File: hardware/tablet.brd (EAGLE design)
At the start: 198 x 124 mm, 16 parts, among them IC2 MCP3201, IC4 MAX6104EUR, IC5 MAX4514EUK

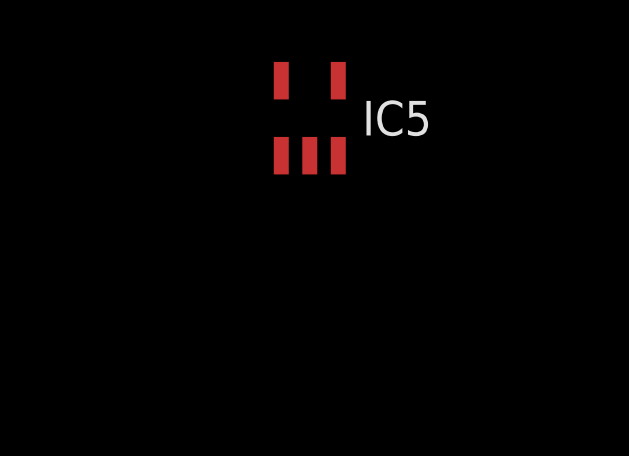
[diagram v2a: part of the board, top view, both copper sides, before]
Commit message: Add protection diodes to common signal
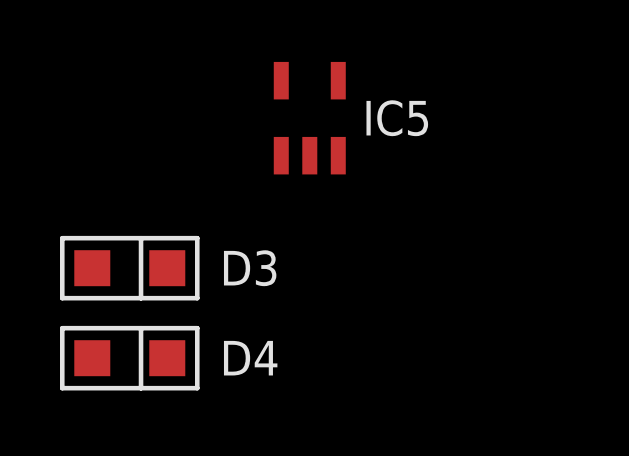
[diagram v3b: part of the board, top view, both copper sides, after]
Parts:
- added D3, D4: 5V1, 0jpe:SOD323
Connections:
- new net N$5: D3.2, D4.2
- net GND: now also D3.1
- net SIG: now also D4.1
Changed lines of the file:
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@@
 <element name="C7" library="0jpe" package="0603" value="100nF" x="-134" y="-122"/>
 <element name="IC5" library="0jpe" package="SOT23_5" value="MAX4514EUK" x="-133" y="-127"/>
+<element name="D3" library="0jpe" package="SOD323" value="5V1" x="-139" y="-132"/>
+<element name="D4" library="0jpe" package="SOD323" value="5V1" x="-139" y="-135"/>
 </elements>
 <signals>
@@
 <signal name="SIG">
 <contactref element="R2" pad="1"/>
+<contactref element="D4" pad="1"/>
+<wire x1="-140.25" y1="-135" x2="-99.75" y2="-88" width="0" layer="19" extent="1-1"/>
 </signal>
 <signal name="GND">
@@
 <contactref element="C7" pad="2"/>
 <contactref element="IC5" pad="3"/>
+<contactref element="D3" pad="1"/>
 <wire x1="-133.25" y1="-116" x2="-133.25" y2="-119" width="0" layer="19" extent="1-1"/>
 <wire x1="-133.25" y1="-122" x2="-133.25" y2="-119" width="0" layer="19" extent="1-1"/>
@@
 <wire x1="-122.365" y1="-94.6" x2="-128.25" y2="-100" width="0" layer="19" extent="1-1"/>
 <wire x1="-121.095" y1="-94.6" x2="-122.365" y2="-94.6" width="0" layer="19" extent="1-1"/>
+<wire x1="-140.25" y1="-132" x2="-132.05" y2="-128.25" width="0" layer="19" extent="1-1"/>
 <wire x1="-113.635" y1="-85.6" x2="-121.095" y2="-94.6" width="0" layer="19" extent="1-1"/>
 <wire x1="-111.095" y1="-80.4" x2="-113.635" y2="-85.6" width="0" layer="19" extent="1-1"/>
@@
 <contactref element="IC5" pad="4"/>
 </signal>
+<signal name="N$5">
+<contactref element="D4" pad="2"/>
+<contactref element="D3" pad="2"/>
+<wire x1="-137.75" y1="-132" x2="-137.75" y2="-135" width="0" layer="19" extent="1-1"/>
+</signal>
 </signals>

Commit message: Fix precision rectifier op amp orientation
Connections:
- net GND: now also IC1.3; no longer IC1.2
- net N$2: now also IC1.2; no longer IC1.3
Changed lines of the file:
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@@
 <setting verticaltext="up"/>
 </settings>
-<grid distance="1" unitdist="mm" unit="mm" style="lines" multiple="1" display="yes" altdistance="0.1" altunitdist="mm" altunit="mm"/>
+<grid distance="1" unitdist="mm" unit="mm" style="lines" multiple="1" display="yes" altdistance="0.0375" altunitdist="mm" altunit="mm"/>
 <layers>
 <layer number="1" name="Top" color="4" fill="1" visible="yes" active="yes"/>
@@
 <wire x1="-90" y1="62" x2="-90" y2="-62" width="0.15" layer="21"/>
 <dimension x1="76" y1="48" x2="76" y2="-48" x3="81" y3="0" textsize="2" layer="47"/>
-<dimension x1="76" y1="-48" x2="-76" y2="-48" x3="0" y3="-53" textsize="2" layer="47"/>
+<dimension x1="76" y1="-48" x2="-76" y2="-47.55" x3="-0.014803125" y3="-52.774978125" textsize="2" layer="47"/>
 <dimension x1="-106" y1="-62" x2="90" y2="-62" x3="-8" y3="-67" textsize="2" layer="47"/>
 <dimension x1="90" y1="-62" x2="90" y2="62" x3="95" y3="0" textsize="2" layer="47"/>
@@
 <contactref element="R2" pad="2"/>
 <contactref element="R1" pad="1"/>
-<contactref element="IC1" pad="3"/>
-<wire x1="-99.75" y1="-85" x2="-112.365" y2="-85.6" width="0" layer="19" extent="1-1"/>
+<contactref element="IC1" pad="2"/>
+<wire x1="-99.75" y1="-85" x2="-113.635" y2="-85.6" width="0" layer="19" extent="1-1"/>
 <wire x1="-98.25" y1="-88" x2="-99.75" y2="-85" width="0" layer="19" extent="1-1"/>
 <wire x1="-98.05" y1="-81.25" x2="-99.75" y2="-85" width="0" layer="19" extent="1-1"/>
-</signal>
-<signal name="N$3">
-<contactref element="D1" pad="3"/>
-<contactref element="IC1" pad="1"/>
-<wire x1="-99" y1="-78.75" x2="-114.905" y2="-85.6" width="0" layer="19" extent="1-1"/>
 </signal>
 <signal name="SIG">
@@
 </signal>
 <signal name="GND">
-<contactref element="IC1" pad="2"/>
 <contactref element="IC1" pad="5"/>
 <contactref element="IC2" pad="3"/>
@@
 <contactref element="IC5" pad="3"/>
 <contactref element="D3" pad="1"/>
+<contactref element="IC1" pad="3"/>
 <wire x1="-133.25" y1="-116" x2="-133.25" y2="-119" width="0" layer="19" extent="1-1"/>
 <wire x1="-133.25" y1="-122" x2="-133.25" y2="-119" width="0" layer="19" extent="1-1"/>
@@
 <wire x1="-121.095" y1="-94.6" x2="-122.365" y2="-94.6" width="0" layer="19" extent="1-1"/>
 <wire x1="-140.25" y1="-132" x2="-132.05" y2="-128.25" width="0" layer="19" extent="1-1"/>
-<wire x1="-113.635" y1="-85.6" x2="-121.095" y2="-94.6" width="0" layer="19" extent="1-1"/>
-<wire x1="-111.095" y1="-80.4" x2="-113.635" y2="-85.6" width="0" layer="19" extent="1-1"/>
+<wire x1="-112.365" y1="-85.6" x2="-121.095" y2="-94.6" width="0" layer="19" extent="1-1"/>
+<wire x1="-111.095" y1="-80.4" x2="-112.365" y2="-85.6" width="0" layer="19" extent="1-1"/>
 </signal>
 <signal name="+5V">
-<contactref element="IC1" pad="8"/>
 <contactref element="C2" pad="1"/>
 <contactref element="C4" pad="1"/>
@@
 <contactref element="C7" pad="1"/>
 <contactref element="IC5" pad="5"/>
+<contactref element="IC1" pad="8"/>
 <wire x1="-134.75" y1="-122" x2="-134.75" y2="-116" width="0" layer="19" extent="1-1"/>
 <wire x1="-133.95" y1="-125.75" x2="-134.75" y2="-122" width="0" layer="19" extent="1-1"/>
@@
 </signal>
 <signal name="-5V">
+<contactref element="C3" pad="2"/>
 <contactref element="IC1" pad="4"/>
-<contactref element="C3" pad="2"/>
 <wire x1="-111.095" y1="-85.6" x2="-128.25" y2="-103" width="0" layer="19" extent="1-1"/>
 </signal>
@@
 <wire x1="-137.75" y1="-132" x2="-137.75" y2="-135" width="0" layer="19" extent="1-1"/>
 </signal>
+<signal name="N$7">
+</signal>
+<signal name="N$8">
+</signal>
+<signal name="N$9">
+</signal>
+<signal name="N$10">
+</signal>
+<signal name="N$11">
+</signal>
+<signal name="N$12">
+</signal>
+<signal name="N$14">
+</signal>
+<signal name="N$15">
+</signal>
+<signal name="N$16">
+</signal>
+<signal name="N$17">
+</signal>
+<signal name="N$18">
+</signal>
+<signal name="N$19">
+</signal>
+<signal name="N$20">
+</signal>
+<signal name="N$21">
+</signal>
+<signal name="N$22">
+</signal>
+<signal name="N$23">
+</signal>
+<signal name="N$24">
+</signal>
+<signal name="N$25">
+</signal>
+<signal name="N$27">
+</signal>
+<signal name="N$3">
+<contactref element="IC1" pad="1"/>
+<contactref element="D1" pad="3"/>
+<wire x1="-99" y1="-78.75" x2="-114.905" y2="-85.6" width="0" layer="19" extent="1-1"/>
+</signal>
 </signals>

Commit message: Draft coil layout
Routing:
- net Y14: track 0.00 -> 2130.9 mm, vias 0 -> 25
- net Y1: track 0.00 -> 2130.9 mm, vias 0 -> 25
- net Y9: track 0.00 -> 2130.9 mm, vias 0 -> 25
- net Y8: track 0.00 -> 2130.9 mm, vias 0 -> 25
- net Y7: track 0.00 -> 2130.9 mm, vias 0 -> 25
- net Y6: track 0.00 -> 2130.9 mm, vias 0 -> 25
- net Y5: track 0.00 -> 2130.9 mm, vias 0 -> 25
- net Y4: track 0.00 -> 2130.9 mm, vias 0 -> 25
- net Y3: track 0.00 -> 2130.9 mm, vias 0 -> 25
- net Y2: track 0.00 -> 2130.9 mm, vias 0 -> 25
- net Y15: track 0.00 -> 2130.9 mm, vias 0 -> 25
- net Y13: track 0.00 -> 2130.9 mm, vias 0 -> 25
- net Y11: track 0.00 -> 2130.9 mm, vias 0 -> 25
- net Y10: track 0.00 -> 2130.9 mm, vias 0 -> 25
- net Y0: track 0.00 -> 2130.9 mm, vias 0 -> 25
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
